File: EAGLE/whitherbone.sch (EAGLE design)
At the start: 215 parts, among them IC1 A4983, IC12 TPS2051BDGN, IC13 SN74AUC1G74, IC14 TPD4S012DRY, IC15 TPD4S012DRY, IC17 SN74LVC2G241DCUR, IC2 SN74LVC1G07DCK, IC4 7805T, IC7 IP4283CZ10-TBR, IC8 IP4283CZ10-TBR, IC9 TDA19988BHN/C1,557, J1 1-1747981-1, Q2 32.768kHz, Q4 24 MHz, T1 BSS138W-7-F, T3 BSS138W-7-F, T4 BSS138W-7-F, U1 OSD3358-512M-BSM, X2 SCHA5B0200, X4 10118192-0001LF

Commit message: Wired up BigEasyDriver
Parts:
- added R28: 47k, 1%, rcl:R-US_R0402
- added R29: 22k, 1%, rcl:R-US_R0402
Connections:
- removed net DIR: IC1.DIR, R22.1
- removed net ENABLE: IC1.ENABLE, R21.1
- removed net MS1: IC1.MS1, R11.1
- removed net MS2: IC1.MS2, R12.1
- removed net MS3: IC1.MS3, R13.1
- removed net RESET: IC1.RESET, R15.1
- removed net SLEEP: IC1.SLEEP, R14.1
- removed net STEP: IC1.STEP, R23.1
- new net DIR(GPIO23): IC1.DIR, R22.1, U1C.GPMC_AD9
- new net ENABLE(GPIO46): IC1.ENABLE, R21.1, U1C.GPMC_AD14
- new net MS1(GPIO27): IC1.MS1, R11.1, U1C.GPMC_AD11
- new net MS2(GPIO44): IC1.MS2, R12.1, U1C.GPMC_AD12
- new net MS3(GPIO45): IC1.MS3, R13.1, U1C.GPMC_AD13
- new net N$49: R28.1, R29.1, U1B.AIN0
- new net RESET(GPIO26): IC1.RESET, R15.1, U1C.GPMC_AD10
- new net SLEEP(GPIO47): IC1.SLEEP, R14.1, U1C.GPMC_AD15
- new net STEP(GPIO22): IC1.STEP, R23.1, U1C.GPMC_AD8
- net CUR_REF: now also R28.2
- net GND: now also R29.2
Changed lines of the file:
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@@
 <part name="JP3" library="SparkFun" deviceset="M04" device="PTH"/>
 <part name="JP5" library="BigEasyDriver_v11" deviceset="M04" device="SCREW_LOCK"/>
+<part name="R28" library="rcl" deviceset="R-US_" device="R0402" value="47k, 1%"/>
+<part name="R29" library="rcl" deviceset="R-US_" device="R0402" value="22k, 1%"/>
+<part name="GND26" library="supply1" deviceset="GND" device=""/>
 </parts>
 <sheets>
@@
 <instance part="JP3" gate="G$1" x="474.98" y="12.7"/>
 <instance part="JP5" gate="G$1" x="502.92" y="12.7"/>
+<instance part="R28" gate="G$1" x="139.7" y="492.76"/>
+<instance part="R29" gate="G$1" x="157.48" y="492.76"/>
+<instance part="GND26" gate="1" x="172.72" y="492.76" rot="R90"/>
 </instances>
 <busses>
@@
 <pinref part="GND25" gate="1" pin="GND"/>
 </segment>
+<segment>
+<pinref part="R29" gate="G$1" pin="2"/>
+<pinref part="GND26" gate="1" pin="GND"/>
+<wire x1="162.56" y1="492.76" x2="170.18" y2="492.76" width="0.1524" layer="91"/>
+</segment>
 </net>
 <net name="N$6" class="0">
@@
 </segment>
 </net>
-<net name="WL_SDIO_D0.SIP" class="0">
-<segment>
-<wire x1="15.24" y1="297.18" x2="58.42" y2="297.18" width="0.1524" layer="91"/>
-<label x="17.78" y="297.18" size="1.778" layer="95"/>
-</segment>
-</net>
-<net name="WL_SDIO_D1.SIP" class="0">
-<segment>
-<wire x1="15.24" y1="294.64" x2="58.42" y2="294.64" width="0.1524" layer="91"/>
-<label x="17.78" y="294.64" size="1.778" layer="95"/>
-</segment>
-</net>
-<net name="WL_SDIO_D2.SIP" class="0">
-<segment>
-<wire x1="15.24" y1="292.1" x2="58.42" y2="292.1" width="0.1524" layer="91"/>
-<label x="17.78" y="292.1" size="1.778" layer="95"/>
-</segment>
-</net>
-<net name="WL_SDIO_D3.SIP" class="0">
-<segment>
-<wire x1="15.24" y1="289.56" x2="58.42" y2="289.56" width="0.1524" layer="91"/>
-<label x="17.78" y="289.56" size="1.778" layer="95"/>
-</segment>
-</net>
-<net name="WL_SDIO_CLK.SIP" class="0">
-<segment>
-<wire x1="15.24" y1="287.02" x2="58.42" y2="287.02" width="0.1524" layer="91"/>
-<label x="17.78" y="287.02" size="1.778" layer="95"/>
-</segment>
-</net>
-<net name="WL_SDIO_CMD.SIP" class="0">
-<segment>
-<wire x1="15.24" y1="284.48" x2="58.42" y2="284.48" width="0.1524" layer="91"/>
-<label x="17.78" y="284.48" size="1.778" layer="95"/>
-</segment>
-</net>
 <net name="N$57" class="0">
 <segment>
@@
 <pinref part="IC1" gate="G$1" pin="REF"/>
 </segment>
+<segment>
+<pinref part="R28" gate="G$1" pin="2"/>
+<wire x1="144.78" y1="492.76" x2="147.32" y2="492.76" width="0.1524" layer="91"/>
+<wire x1="147.32" y1="492.76" x2="147.32" y2="502.92" width="0.1524" layer="91"/>
+<wire x1="147.32" y1="502.92" x2="170.18" y2="502.92" width="0.1524" layer="91"/>
+<label x="162.56" y="502.92" size="1.778" layer="95"/>
+</segment>
 </net>
 <net name="COILB+" class="0">
@@
 </segment>
 </net>
-<net name="DIR" class="0">
+<net name="DIR(GPIO23)" class="0">
 <segment>
 <wire x1="467.36" y1="60.96" x2="449.58" y2="60.96" width="0.1524" layer="91"/>
-<label x="452.12" y="61.468" size="1.778" layer="95"/>
+<label x="449.58" y="61.468" size="1.778" layer="95"/>
 <pinref part="IC1" gate="G$1" pin="DIR"/>
 </segment>
@@
 <pinref part="R22" gate="G$1" pin="1"/>
 </segment>
+<segment>
+<wire x1="655.32" y1="462.28" x2="637.54" y2="462.28" width="0.1524" layer="91"/>
+<label x="640.08" y="462.788" size="1.778" layer="95"/>
+<pinref part="U1" gate="C" pin="GPMC_AD9"/>
+</segment>
 </net>
-<net name="MS1" class="0">
+<net name="MS1(GPIO27)" class="0">
 <segment>
 <wire x1="467.36" y1="55.88" x2="449.58" y2="55.88" width="0.1524" layer="91"/>
-<label x="452.12" y="56.388" size="1.778" layer="95"/>
+<label x="449.58" y="56.388" size="1.778" layer="95"/>
 <pinref part="IC1" gate="G$1" pin="MS1"/>
 </segment>
@@
 <pinref part="R11" gate="G$1" pin="1"/>
 </segment>
+<segment>
+<wire x1="655.32" y1="457.2" x2="637.54" y2="457.2" width="0.1524" layer="91"/>
+<label x="640.08" y="457.708" size="1.778" layer="95"/>
+<pinref part="U1" gate="C" pin="GPMC_AD11"/>
+</segment>
 </net>
-<net name="MS2" class="0">
+<net name="MS2(GPIO44)" class="0">
 <segment>
 <wire x1="467.36" y1="53.34" x2="449.58" y2="53.34" width="0.1524" layer="91"/>
-<label x="452.12" y="53.848" size="1.778" layer="95"/>
+<label x="449.58" y="53.848" size="1.778" layer="95"/>
 <pinref part="IC1" gate="G$1" pin="MS2"/>
 </segment>
@@
 <pinref part="R12" gate="G$1" pin="1"/>
 </segment>
+<segment>
+<wire x1="655.32" y1="454.66" x2="637.54" y2="454.66" width="0.1524" layer="91"/>
+<label x="640.08" y="455.168" size="1.778" layer="95"/>
+<pinref part="U1" gate="C" pin="GPMC_AD12"/>
+</segment>
 </net>
-<net name="ENABLE" class="0">
+<net name="ENABLE(GPIO46)" class="0">
 <segment>
 <wire x1="467.36" y1="48.26" x2="449.58" y2="48.26" width="0.1524" layer="91"/>
-<label x="452.12" y="48.768" size="1.778" layer="95"/>
+<label x="449.58" y="48.768" size="1.778" layer="95"/>
 <pinref part="IC1" gate="G$1" pin="ENABLE"/>
 </segment>
@@
 <pinref part="R21" gate="G$1" pin="1"/>
 </segment>
+<segment>
+<wire x1="655.32" y1="449.58" x2="637.54" y2="449.58" width="0.1524" layer="91"/>
+<label x="640.08" y="450.088" size="1.778" layer="95"/>
+<pinref part="U1" gate="C" pin="GPMC_AD14"/>
+</segment>
 </net>
 <net name="COILA-" class="0">
@@
 </segment>
 </net>
-<net name="RESET" class="0">
+<net name="RESET(GPIO26)" class="0">
 <segment>
 <wire x1="467.36" y1="58.42" x2="449.58" y2="58.42" width="0.1524" layer="91"/>
-<label x="452.12" y="58.928" size="1.778" layer="95"/>
+<label x="449.58" y="58.928" size="1.778" layer="95"/>
 <pinref part="IC1" gate="G$1" pin="RESET"/>
 </segment>
@@
 <pinref part="R15" gate="G$1" pin="1"/>
 </segment>
+<segment>
+<wire x1="655.32" y1="459.74" x2="637.54" y2="459.74" width="0.1524" layer="91"/>
+<label x="640.08" y="460.248" size="1.778" layer="95"/>
+<pinref part="U1" gate="C" pin="GPMC_AD10"/>
+</segment>
 </net>
-<net name="STEP" class="0">
+<net name="STEP(GPIO22)" class="0">
 <segment>
 <wire x1="467.36" y1="63.5" x2="449.58" y2="63.5" width="0.1524" layer="91"/>
-<label x="452.12" y="64.008" size="1.778" layer="95"/>
+<label x="449.58" y="64.008" size="1.778" layer="95"/>
 <pinref part="IC1" gate="G$1" pin="STEP"/>
 </segment>
@@
 <pinref part="R23" gate="G$1" pin="1"/>
 </segment>
+<segment>
+<wire x1="655.32" y1="464.82" x2="637.54" y2="464.82" width="0.1524" layer="91"/>
+<label x="640.08" y="465.328" size="1.778" layer="95"/>
+<pinref part="U1" gate="C" pin="GPMC_AD8"/>
+</segment>
 </net>
-<net name="SLEEP" class="0">
+<net name="SLEEP(GPIO47)" class="0">
 <segment>
 <wire x1="467.36" y1="45.72" x2="449.58" y2="45.72" width="0.1524" layer="91"/>
-<label x="452.12" y="46.228" size="1.778" layer="95"/>
+<label x="449.58" y="46.228" size="1.778" layer="95"/>
 <pinref part="IC1" gate="G$1" pin="SLEEP"/>
 </segment>
@@
 <pinref part="R14" gate="G$1" pin="1"/>
 </segment>
+<segment>
+<wire x1="655.32" y1="447.04" x2="637.54" y2="447.04" width="0.1524" layer="91"/>
+<label x="640.08" y="447.548" size="1.778" layer="95"/>
+<pinref part="U1" gate="C" pin="GPMC_AD15"/>
+</segment>
 </net>
 <net name="N$31" class="0">
@@
 </segment>
 </net>
-<net name="MS3" class="0">
+<net name="MS3(GPIO45)" class="0">
 <segment>
 <wire x1="467.36" y1="50.8" x2="449.58" y2="50.8" width="0.1524" layer="91"/>
-<label x="452.12" y="51.308" size="1.778" layer="95"/>
+<label x="449.58" y="51.308" size="1.778" layer="95"/>
 <pinref part="IC1" gate="G$1" pin="MS3"/>
 </segment>
@@
 <pinref part="R13" gate="G$1" pin="1"/>
 </segment>
+<segment>
+<wire x1="655.32" y1="452.12" x2="637.54" y2="452.12" width="0.1524" layer="91"/>
+<label x="640.08" y="452.628" size="1.778" layer="95"/>
+<pinref part="U1" gate="C" pin="GPMC_AD13"/>
+</segment>
 </net>
 <net name="N$48" class="0">
@@
 </segment>
 </net>
+<net name="N$49" class="0">
+<segment>
+<pinref part="U1" gate="B" pin="AIN0"/>
+<pinref part="R28" gate="G$1" pin="1"/>
+<wire x1="129.54" y1="492.76" x2="132.08" y2="492.76" width="0.1524" layer="91"/>
+<wire x1="132.08" y1="492.76" x2="134.62" y2="492.76" width="0.1524" layer="91"/>
+<wire x1="132.08" y1="492.76" x2="132.08" y2="487.68" width="0.1524" layer="91"/>
+<pinref part="R29" gate="G$1" pin="1"/>
+<wire x1="132.08" y1="487.68" x2="152.4" y2="487.68" width="0.1524" layer="91"/>
+<wire x1="152.4" y1="487.68" x2="152.4" y2="492.76" width="0.1524" layer="91"/>
+<junction x="132.08" y="492.76"/>
+</segment>
+</net>

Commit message: Add connector for Neopixels (not yet connected)
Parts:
- added JP1: (no value), SparkFun:M04PTH
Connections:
- new net TO_NEOPIXEL: U1C.MCASP0_AXR0
- net GND: now also JP1.1
- net VDD_5V: now also JP1.4
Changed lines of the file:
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@@
 <part name="R29" library="rcl" deviceset="R-US_" device="R0402" value="22k, 1%"/>
 <part name="GND26" library="supply1" deviceset="GND" device=""/>
+<part name="JP1" library="SparkFun" deviceset="M04" device="PTH"/>
+<part name="GND27" library="supply1" deviceset="GND" device=""/>
+<part name="SUPPLY10" library="GHI-PowerGoundSupply" deviceset="VDD_5V" device=""/>
 </parts>
 <sheets>
@@
 <instance part="R29" gate="G$1" x="157.48" y="492.76"/>
 <instance part="GND26" gate="1" x="172.72" y="492.76" rot="R90"/>
+<instance part="JP1" gate="G$1" x="670.56" y="114.3"/>
+<instance part="GND27" gate="1" x="688.34" y="106.68"/>
+<instance part="SUPPLY10" gate="G$1" x="688.34" y="124.46"/>
 </instances>
 <busses>
@@
 <wire x1="162.56" y1="492.76" x2="170.18" y2="492.76" width="0.1524" layer="91"/>
 </segment>
+<segment>
+<pinref part="JP1" gate="G$1" pin="1"/>
+<wire x1="675.64" y1="111.76" x2="688.34" y2="111.76" width="0.1524" layer="91"/>
+<label x="678.18" y="111.76" size="1.778" layer="95"/>
+<pinref part="GND27" gate="1" pin="GND"/>
+<wire x1="688.34" y1="111.76" x2="688.34" y2="109.22" width="0.1524" layer="91"/>
+</segment>
 </net>
 <net name="N$6" class="0">
@@
 <wire x1="414.02" y1="76.2" x2="421.64" y2="76.2" width="0.1524" layer="91"/>
 </segment>
+<segment>
+<pinref part="JP1" gate="G$1" pin="4"/>
+<wire x1="675.64" y1="119.38" x2="688.34" y2="119.38" width="0.1524" layer="91"/>
+<wire x1="688.34" y1="119.38" x2="688.34" y2="121.92" width="0.1524" layer="91"/>
+<label x="678.18" y="119.38" size="1.778" layer="95"/>
+<pinref part="SUPPLY10" gate="G$1" pin="VDD_5V"/>
+</segment>
 </net>
 <net name="PWR_BUT" class="0">
@@
 </segment>
 </net>
+<net name="TO_NEOPIXEL" class="0">
+<segment>
+<pinref part="U1" gate="C" pin="MCASP0_AXR0"/>
+<wire x1="568.96" y1="474.98" x2="535.94" y2="474.98" width="0.1524" layer="91"/>
+<label x="538.48" y="474.98" size="1.778" layer="95"/>
+</segment>
+</net>

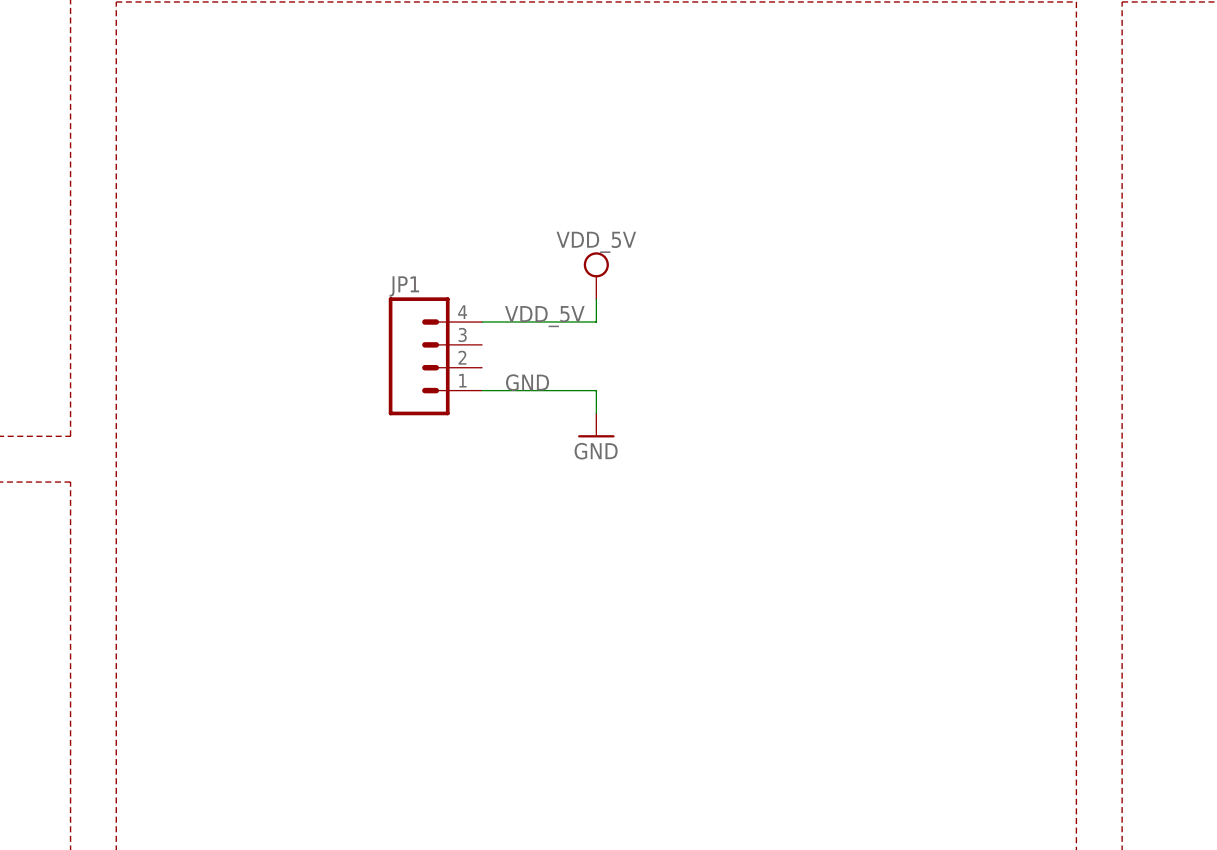
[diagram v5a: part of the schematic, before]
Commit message: Connected NEOPIXEL connector
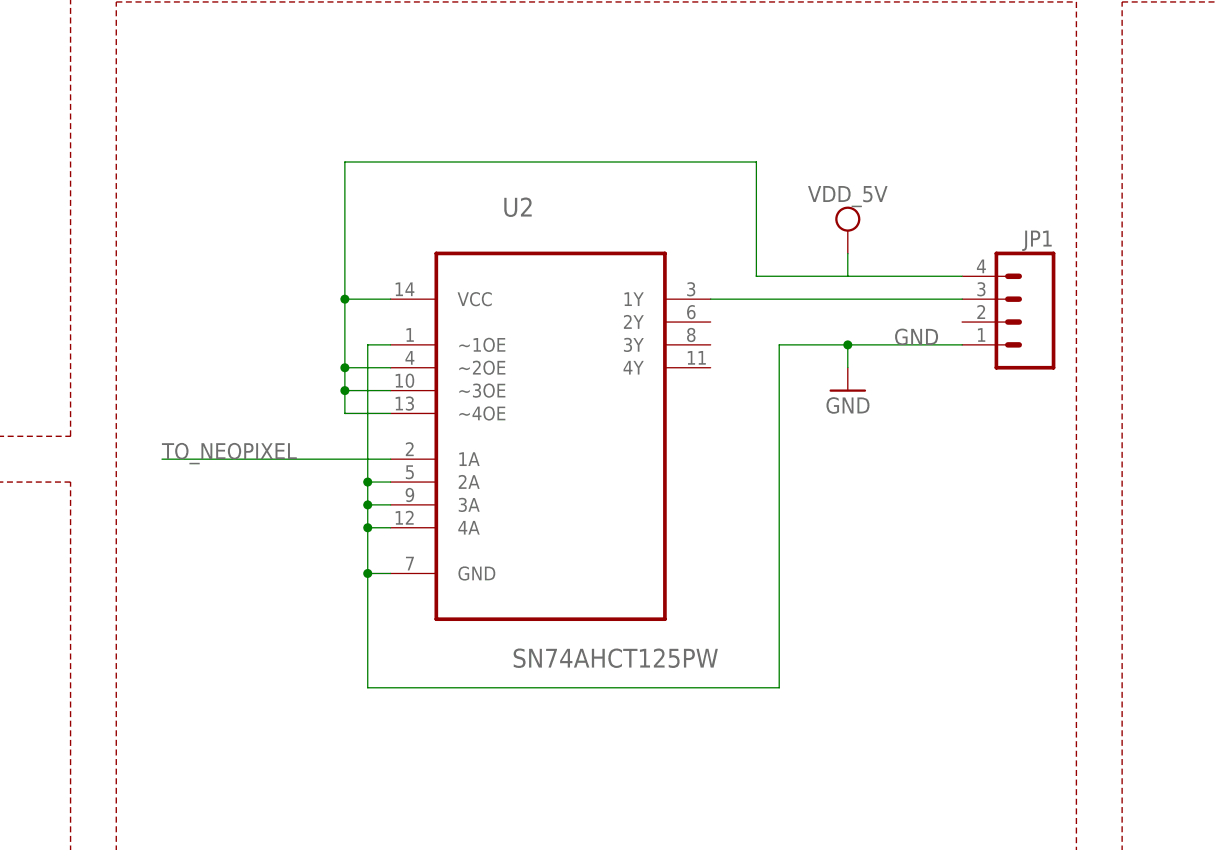
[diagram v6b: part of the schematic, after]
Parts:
- added U2: SN74AHCT125PW, SN74AHCT125PW:SN74AHCT125PW
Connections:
- new net N$51: JP1.3, U2.1Y
- net GND: now also U2.2A, U2.3A, U2.4A, U2.GND, U2.~1OE
- net TO_NEOPIXEL: now also U2.1A
- net VDD_5V: now also U2.VCC, U2.~2OE, U2.~3OE, U2.~4OE
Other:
- moved on the sheet: JP1
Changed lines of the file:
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@@
 <part name="GND27" library="supply1" deviceset="GND" device=""/>
 <part name="SUPPLY10" library="GHI-PowerGoundSupply" deviceset="VDD_5V" device=""/>
+<part name="U2" library="SN74AHCT125PW" deviceset="SN74AHCT125PW" device=""/>
 </parts>
 <sheets>
@@
 <instance part="R29" gate="G$1" x="157.48" y="492.76"/>
 <instance part="GND26" gate="1" x="172.72" y="492.76" rot="R90"/>
-<instance part="JP1" gate="G$1" x="670.56" y="114.3"/>
-<instance part="GND27" gate="1" x="688.34" y="106.68"/>
-<instance part="SUPPLY10" gate="G$1" x="688.34" y="124.46"/>
+<instance part="JP1" gate="G$1" x="734.06" y="119.38" rot="MR0"/>
+<instance part="GND27" gate="1" x="716.28" y="111.76" rot="MR0"/>
+<instance part="SUPPLY10" gate="G$1" x="716.28" y="129.54" rot="MR0"/>
+<instance part="U2" gate="A" x="683.26" y="109.22"/>
 </instances>
 <busses>
@@
 <segment>
 <pinref part="JP1" gate="G$1" pin="1"/>
-<wire x1="675.64" y1="111.76" x2="688.34" y2="111.76" width="0.1524" layer="91"/>
-<label x="678.18" y="111.76" size="1.778" layer="95"/>
+<wire x1="728.98" y1="116.84" x2="716.28" y2="116.84" width="0.1524" layer="91"/>
+<label x="726.44" y="116.84" size="1.778" layer="95" rot="MR0"/>
 <pinref part="GND27" gate="1" pin="GND"/>
-<wire x1="688.34" y1="111.76" x2="688.34" y2="109.22" width="0.1524" layer="91"/>
+<wire x1="716.28" y1="116.84" x2="716.28" y2="114.3" width="0.1524" layer="91"/>
+<wire x1="716.28" y1="116.84" x2="708.66" y2="116.84" width="0.1524" layer="91"/>
+<junction x="716.28" y="116.84"/>
+<pinref part="U2" gate="A" pin="GND"/>
+<wire x1="665.48" y1="91.44" x2="662.94" y2="91.44" width="0.1524" layer="91"/>
+<wire x1="662.94" y1="91.44" x2="662.94" y2="78.74" width="0.1524" layer="91"/>
+<wire x1="662.94" y1="78.74" x2="708.66" y2="78.74" width="0.1524" layer="91"/>
+<wire x1="708.66" y1="78.74" x2="708.66" y2="116.84" width="0.1524" layer="91"/>
+<pinref part="U2" gate="A" pin="~1OE"/>
+<wire x1="665.48" y1="116.84" x2="662.94" y2="116.84" width="0.1524" layer="91"/>
+<wire x1="662.94" y1="116.84" x2="662.94" y2="101.6" width="0.1524" layer="91"/>
+<pinref part="U2" gate="A" pin="2A"/>
+<wire x1="662.94" y1="101.6" x2="662.94" y2="99.06" width="0.1524" layer="91"/>
+<wire x1="662.94" y1="99.06" x2="662.94" y2="96.52" width="0.1524" layer="91"/>
+<wire x1="662.94" y1="96.52" x2="662.94" y2="91.44" width="0.1524" layer="91"/>
+<wire x1="662.94" y1="101.6" x2="665.48" y2="101.6" width="0.1524" layer="91"/>
+<pinref part="U2" gate="A" pin="3A"/>
+<wire x1="662.94" y1="99.06" x2="665.48" y2="99.06" width="0.1524" layer="91"/>
+<pinref part="U2" gate="A" pin="4A"/>
+<wire x1="662.94" y1="96.52" x2="665.48" y2="96.52" width="0.1524" layer="91"/>
+<junction x="662.94" y="91.44"/>
+<junction x="662.94" y="96.52"/>
+<junction x="662.94" y="99.06"/>
+<junction x="662.94" y="101.6"/>
 </segment>
 </net>
@@
 </segment>
 <segment>
-<pinref part="JP1" gate="G$1" pin="4"/>
-<wire x1="675.64" y1="119.38" x2="688.34" y2="119.38" width="0.1524" layer="91"/>
-<wire x1="688.34" y1="119.38" x2="688.34" y2="121.92" width="0.1524" layer="91"/>
-<label x="678.18" y="119.38" size="1.778" layer="95"/>
+<wire x1="716.28" y1="124.46" x2="716.28" y2="127" width="0.1524" layer="91"/>
 <pinref part="SUPPLY10" gate="G$1" pin="VDD_5V"/>
+<wire x1="706.12" y1="137.16" x2="706.12" y2="124.46" width="0.1524" layer="91"/>
+<wire x1="706.12" y1="124.46" x2="716.28" y2="124.46" width="0.1524" layer="91"/>
+<pinref part="JP1" gate="G$1" pin="4"/>
+<wire x1="716.28" y1="124.46" x2="728.98" y2="124.46" width="0.1524" layer="91"/>
+<pinref part="U2" gate="A" pin="VCC"/>
+<wire x1="665.48" y1="121.92" x2="660.4" y2="121.92" width="0.1524" layer="91"/>
+<wire x1="660.4" y1="121.92" x2="660.4" y2="137.16" width="0.1524" layer="91"/>
+<wire x1="660.4" y1="137.16" x2="706.12" y2="137.16" width="0.1524" layer="91"/>
+<wire x1="660.4" y1="121.92" x2="660.4" y2="114.3" width="0.1524" layer="91"/>
+<pinref part="U2" gate="A" pin="~2OE"/>
+<wire x1="660.4" y1="114.3" x2="665.48" y2="114.3" width="0.1524" layer="91"/>
+<wire x1="660.4" y1="114.3" x2="660.4" y2="111.76" width="0.1524" layer="91"/>
+<pinref part="U2" gate="A" pin="~3OE"/>
+<wire x1="660.4" y1="111.76" x2="665.48" y2="111.76" width="0.1524" layer="91"/>
+<wire x1="660.4" y1="111.76" x2="660.4" y2="109.22" width="0.1524" layer="91"/>
+<pinref part="U2" gate="A" pin="~4OE"/>
+<wire x1="660.4" y1="109.22" x2="665.48" y2="109.22" width="0.1524" layer="91"/>
+<junction x="660.4" y="114.3"/>
+<junction x="660.4" y="111.76"/>
+<junction x="660.4" y="121.92"/>
 </segment>
 </net>
@@
 <label x="538.48" y="474.98" size="1.778" layer="95"/>
 </segment>
+<segment>
+<pinref part="U2" gate="A" pin="1A"/>
+<wire x1="665.48" y1="104.14" x2="640.08" y2="104.14" width="0.1524" layer="91"/>
+<label x="640.08" y="104.14" size="1.778" layer="95"/>
+</segment>
+</net>
+<net name="N$51" class="0">
+<segment>
+<pinref part="JP1" gate="G$1" pin="3"/>
+<wire x1="728.98" y1="121.92" x2="701.04" y2="121.92" width="0.1524" layer="91"/>
+<pinref part="U2" gate="A" pin="1Y"/>
+</segment>
 </net>
